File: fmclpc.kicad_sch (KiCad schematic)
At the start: 3 parts, among them J1401 ASP-134604-01, J1402 ASP-134604-01

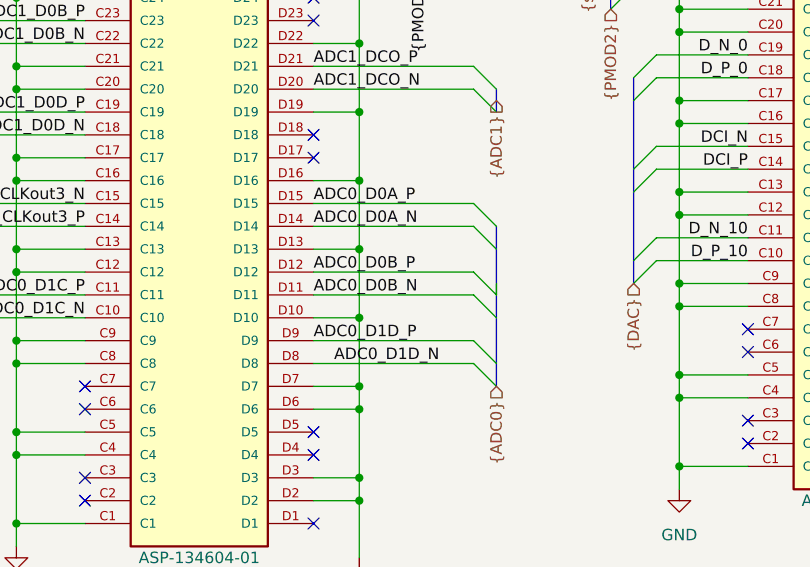
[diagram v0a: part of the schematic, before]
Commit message: Updates from Michal to fix ERC errors
Still lots of ERC warnings
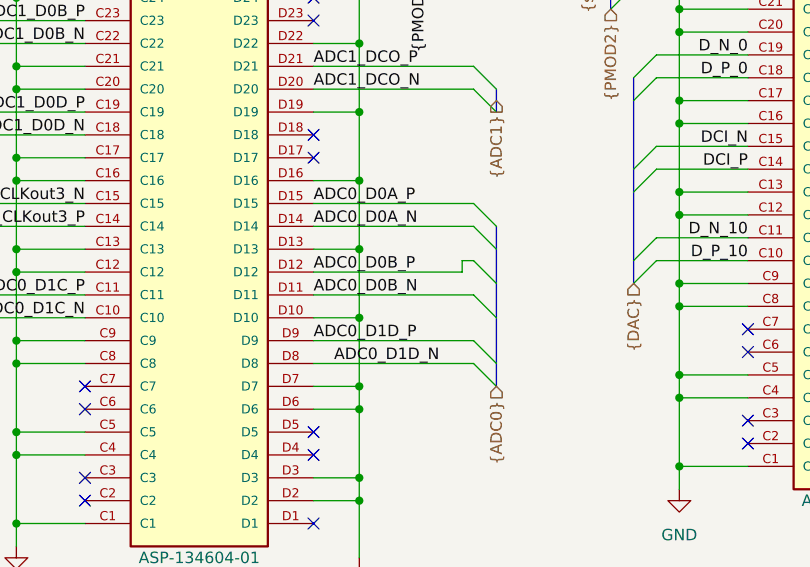
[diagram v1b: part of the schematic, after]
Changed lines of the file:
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@@
 	)
 	(bus_entry
-		(at 104.14 215.9)
+		(at 104.14 214.63)
 		(size -2.54 -2.54)
 		(stroke
@@
 	(wire
 		(pts
-			(xy 104.14 215.9) (xy 104.14 214.63)
-		)
-		(stroke
-			(width 0)
-			(type default)
-		)
-	)
-	(wire
-		(pts
 			(xy 124.46 224.79) (xy 124.46 217.17)
 		)
@@
 	(wire
 		(pts
-			(xy 101.6 213.36) (xy 83.82 213.36)
+			(xy 101.6 212.09) (xy 100.33 212.09)
 		)
 		(stroke
@@
 	(bus
 		(pts
-			(xy 104.14 218.44) (xy 104.14 215.9)
+			(xy 104.14 218.44) (xy 104.14 214.63)
 		)
 		(stroke
@@
 	(wire
 		(pts
+			(xy 100.33 213.36) (xy 83.82 213.36)
+		)
+		(stroke
+			(width 0)
+			(type default)
+		)
+	)
+	(wire
+		(pts
 			(xy 83.82 187.96) (xy 88.9 187.96)
 		)
@@
 	(bus
 		(pts
-			(xy 104.14 215.9) (xy 104.14 210.82)
+			(xy 104.14 214.63) (xy 104.14 210.82)
 		)
 		(stroke
@@
 		)
 		(stroke
+			(width 0)
+			(type default)
+		)
+	)
+	(wire
+		(pts
+			(xy 100.33 212.09) (xy 100.33 213.36)
+		)
+		(stroke
